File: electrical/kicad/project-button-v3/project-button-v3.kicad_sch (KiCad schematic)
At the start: 0 parts

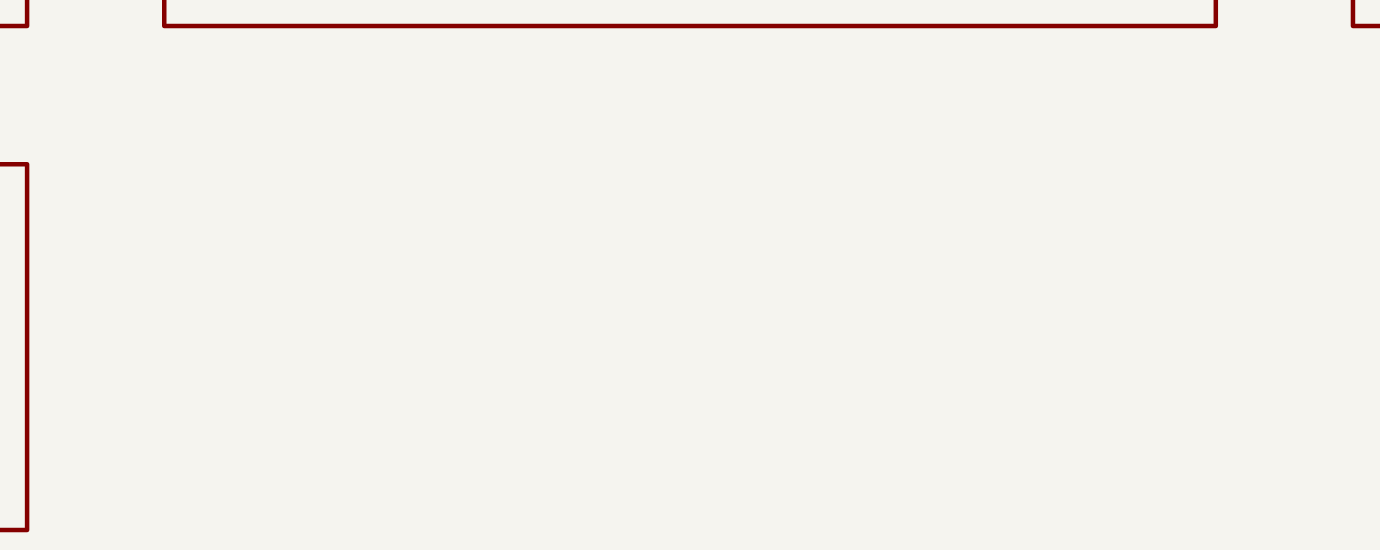
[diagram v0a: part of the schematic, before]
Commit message: Add native watchdog PCB placement candidate
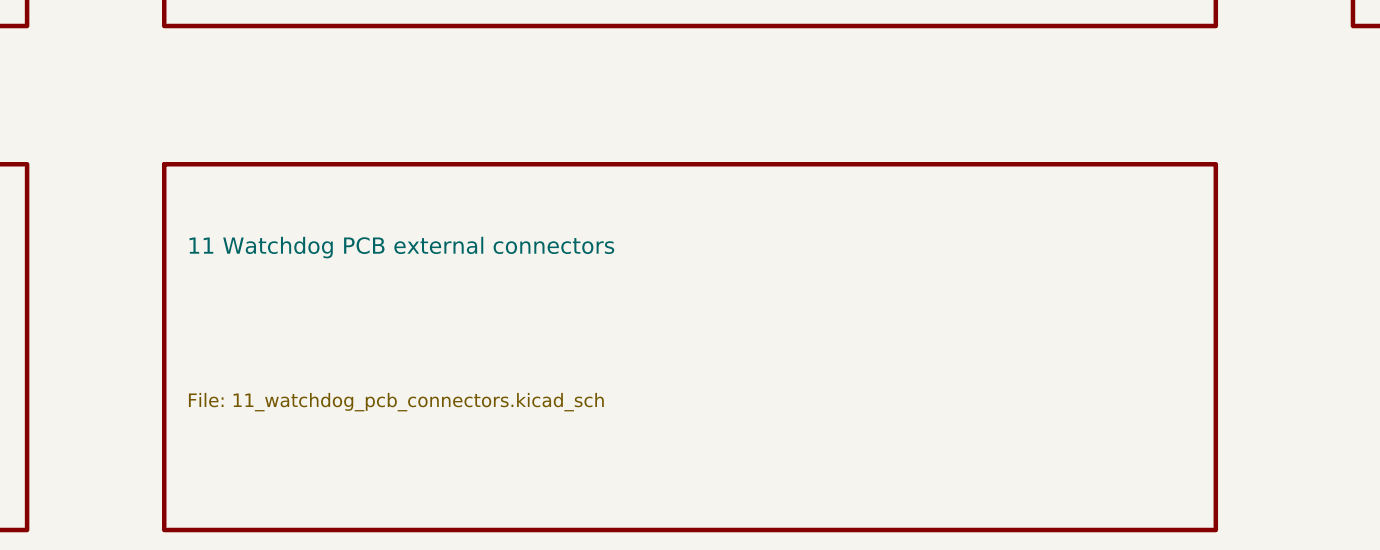
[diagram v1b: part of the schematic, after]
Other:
- added sheet 11 Watchdog PCB external connectors (11_watchdog_pcb_connectors.kicad_sch)
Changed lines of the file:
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@@
 (kicad_sch
   (version 20250114) (generator "eeschema") (generator_version "10.0") (paper "A3")
-  (title_block (title "Project Button HR-V0 Electrical V3 index") (date "2026-08-06") (rev "V3-P0.9")
+  (title_block (title "Project Button HR-V0 Electrical V3 index") (date "2026-08-06") (rev "V3-P1.0")
     (company "Project Button") (comment 1 "PRELIMINARY - NOT APPROVED FOR FABRICATION OR ENERGIZATION") (comment 2 "V2.1 PRESERVED; V3 IS A CONNECTED CANDIDATE"))
   (text "PRELIMINARY - NOT APPROVED FOR FABRICATION OR ENERGIZATION" (exclude_from_sim no) (at 17.78 10.16 0)
@@
           (property "Sheetname" "10 U2D2, actuator ports and bonding boundary" (at 20.32 220.16 0) (effects (font (size 1.80 1.80)) (justify left bottom)))
           (property "Sheetfile" "10_actuator_interfaces.kicad_sch" (at 20.32 235.40 0) (effects (font (size 1.50 1.50)) (justify left top)))
-          (instances (project "project-button-v3" (path "/5cd52082-c883-51c8-b492-8b3b3e331e69" (page "11")))))
+          (instances (project "project-button-v3" (path "/5cd52082-c883-51c8-b492-8b3b3e331e69" (page "11"))))) (sheet (at 149.86 210.00) (size 116.84 40.64)
+          (exclude_from_sim no) (in_bom yes) (on_board yes) (dnp no)
+          (stroke (width 0.5) (type solid)) (fill (color 0 0 0 0.0000))
+          (property "Sheetname" "11 Watchdog PCB external connectors" (at 152.40 220.16 0) (effects (font (size 1.80 1.80)) (justify left bottom)))
+          (property "Sheetfile" "11_watchdog_pcb_connectors.kicad_sch" (at 152.40 235.40 0) (effects (font (size 1.50 1.50)) (justify left top)))
+          (instances (project "project-button-v3" (path "/5cd52082-c883-51c8-b492-8b3b3e331e69" (page "12")))))
   (sheet_instances (path "/" (page "1"))) (embedded_fonts no))

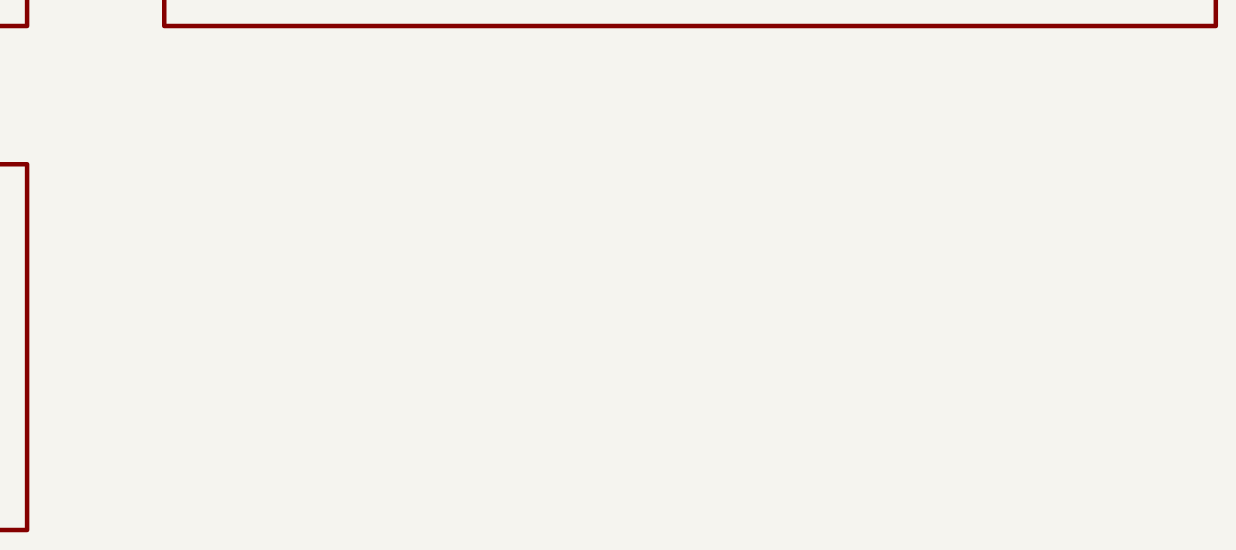
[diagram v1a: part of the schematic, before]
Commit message: Add watchdog PCB test access and SUB copper
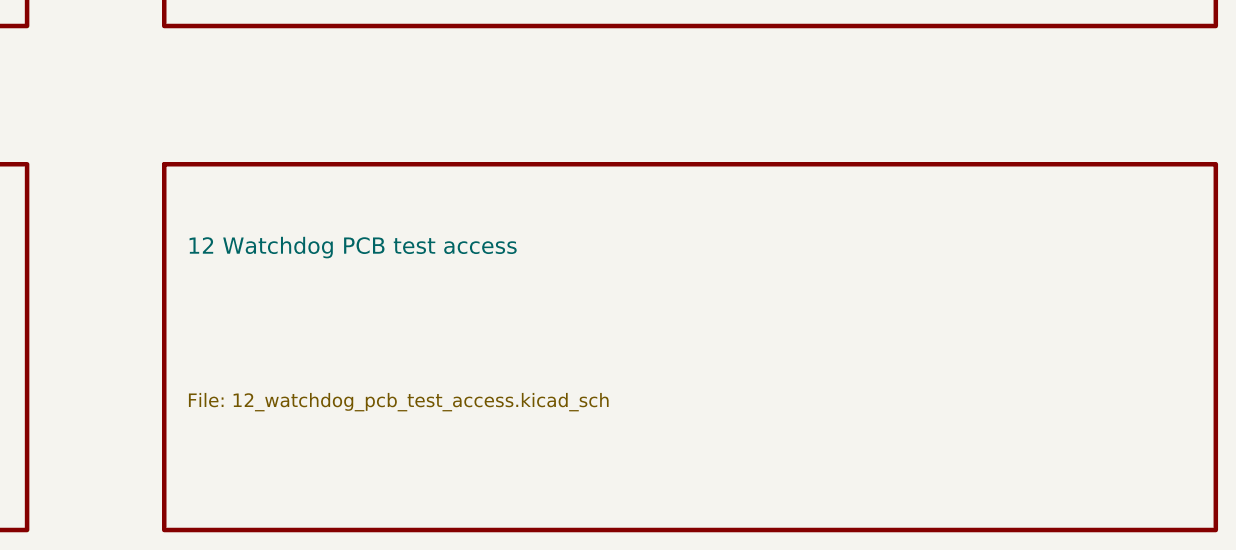
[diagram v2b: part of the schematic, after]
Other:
- added sheet 12 Watchdog PCB test access (12_watchdog_pcb_test_access.kicad_sch)
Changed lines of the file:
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@@
 (kicad_sch
   (version 20250114) (generator "eeschema") (generator_version "10.0") (paper "A3")
-  (title_block (title "Project Button HR-V0 Electrical V3 index") (date "2026-08-06") (rev "V3-P1.0")
+  (title_block (title "Project Button HR-V0 Electrical V3 index") (date "2026-08-06") (rev "V3-P1.1")
     (company "Project Button") (comment 1 "PRELIMINARY - NOT APPROVED FOR FABRICATION OR ENERGIZATION") (comment 2 "V2.1 PRESERVED; V3 IS A CONNECTED CANDIDATE"))
   (text "PRELIMINARY - NOT APPROVED FOR FABRICATION OR ENERGIZATION" (exclude_from_sim no) (at 17.78 10.16 0)
@@
           (property "Sheetname" "11 Watchdog PCB external connectors" (at 152.40 220.16 0) (effects (font (size 1.80 1.80)) (justify left bottom)))
           (property "Sheetfile" "11_watchdog_pcb_connectors.kicad_sch" (at 152.40 235.40 0) (effects (font (size 1.50 1.50)) (justify left top)))
-          (instances (project "project-button-v3" (path "/5cd52082-c883-51c8-b492-8b3b3e331e69" (page "12")))))
+          (instances (project "project-button-v3" (path "/5cd52082-c883-51c8-b492-8b3b3e331e69" (page "12"))))) (sheet (at 281.94 210.00) (size 116.84 40.64)
+          (exclude_from_sim no) (in_bom yes) (on_board yes) (dnp no)
+          (stroke (width 0.5) (type solid)) (fill (color 0 0 0 0.0000))
+          (property "Sheetname" "12 Watchdog PCB test access" (at 284.48 220.16 0) (effects (font (size 1.80 1.80)) (justify left bottom)))
+          (property "Sheetfile" "12_watchdog_pcb_test_access.kicad_sch" (at 284.48 235.40 0) (effects (font (size 1.50 1.50)) (justify left top)))
+          (instances (project "project-button-v3" (path "/5cd52082-c883-51c8-b492-8b3b3e331e69" (page "13")))))
   (sheet_instances (path "/" (page "1"))) (embedded_fonts no))

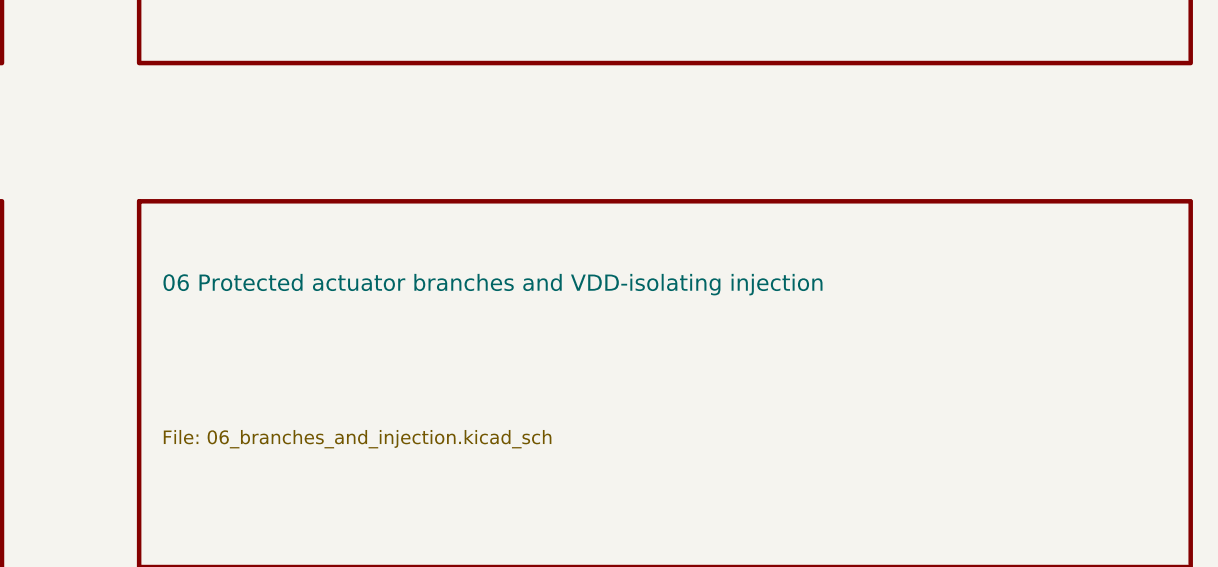
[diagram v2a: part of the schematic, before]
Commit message: Add native DYNAMIXEL star injection release candidate
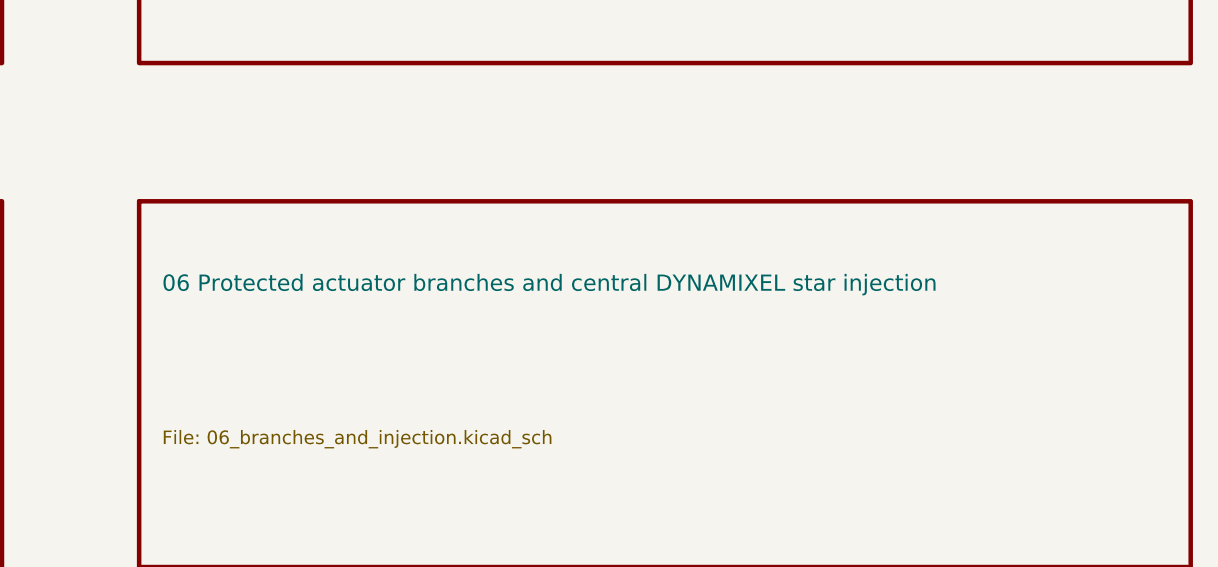
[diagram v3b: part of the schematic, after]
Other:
- sheet 06 Protected actuator branches and VDD-isolating injection renamed 06 Protected actuator branches and central DYNAMIXEL star injection
- title: Project Button HR-V0 Electrical V3 index -> PROJECT BUTTON HR-V0 ELECTRICAL V3 CONNECTED CANDIDATE index
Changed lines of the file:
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@@
 (kicad_sch
   (version 20250114) (generator "eeschema") (generator_version "10.0") (paper "A3")
-  (title_block (title "Project Button HR-V0 Electrical V3 index") (date "2026-08-06") (rev "V3-P1.1")
+  (title_block (title "PROJECT BUTTON HR-V0 ELECTRICAL V3 CONNECTED CANDIDATE index") (date "2026-08-07") (rev "V3-P1.2")
     (company "Project Button") (comment 1 "PRELIMINARY - NOT APPROVED FOR FABRICATION OR ENERGIZATION") (comment 2 "V2.1 PRESERVED; V3 IS A CONNECTED CANDIDATE"))
   (text "PRELIMINARY - NOT APPROVED FOR FABRICATION OR ENERGIZATION" (exclude_from_sim no) (at 17.78 10.16 0)
@@
           (exclude_from_sim no) (in_bom yes) (on_board yes) (dnp no)
           (stroke (width 0.5) (type solid)) (fill (color 0 0 0 0.0000))
-          (property "Sheetname" "06 Protected actuator branches and VDD-isolating injection" (at 284.48 108.16 0) (effects (font (size 1.80 1.80)) (justify left bottom)))
+          (property "Sheetname" "06 Protected actuator branches and central DYNAMIXEL star injection" (at 284.48 108.16 0) (effects (font (size 1.80 1.80)) (justify left bottom)))
           (property "Sheetfile" "06_branches_and_injection.kicad_sch" (at 284.48 123.40 0) (effects (font (size 1.50 1.50)) (justify left top)))
           (instances (project "project-button-v3" (path "/5cd52082-c883-51c8-b492-8b3b3e331e69" (page "7"))))) (sheet (at 17.78 154.00) (size 116.84 40.64)
